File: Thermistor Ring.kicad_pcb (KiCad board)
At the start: 2 copper layers, 48.3 x 48.3 mm, 15 parts, among them J1 Conn_01x04_Socket, U2 MCP9808T-E/MC, U3 MCP9808T-E/MC, U4 MCP9808T-E/MC, U5 MCP9808T-E/MC, U6 MCP9808T-E/MC, U7 MCP9808T-E/MC

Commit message: Ouptut adjustments
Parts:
- U2, U3, U4, U5, U6, U7: footprint MCP9808-E/MS:MSOP8_MC_MCH -> MCP9808-E/MS:MSOP8_MC_MCH_SMALL_PADS
- moved C1 2.72 mm to (77.9, 76.2)
- moved R3 2.46 mm to (58.7, 41.2)
- moved C5 2.02 mm to (59.5, 70.2)
- moved C6 1.95 mm to (93.0, 62.8)
- moved U6 1.24 mm to (64.2, 73.4)
- moved U4 1.24 mm to (83.4, 73.5)
- moved C3 1.24 mm to (63.6, 37.5)
- moved U3 1.24 mm to (54.6, 57.0)
- moved C4 1.24 mm to (87.5, 43.2)
- moved U7 1.24 mm to (83.2, 40.5)
- moved J1 1.24 mm to (69.9, 37.7)
- moved U2 1.24 mm to (64.2, 40.4)
- moved U5 1.24 mm to (92.8, 57.0)
- moved R2 1.10 mm to (82.8, 36.4), turned to 180 degrees
- moved C2 1.06 mm to (54.7, 52.1)
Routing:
- net /Power 3.3-5V: track 204.1 -> 213.8 mm
- net /SCL: track 123.0 -> 124.4 mm
- net /SDA: track 169.3 -> 170.2 mm
- net GND: vias 77 -> 79

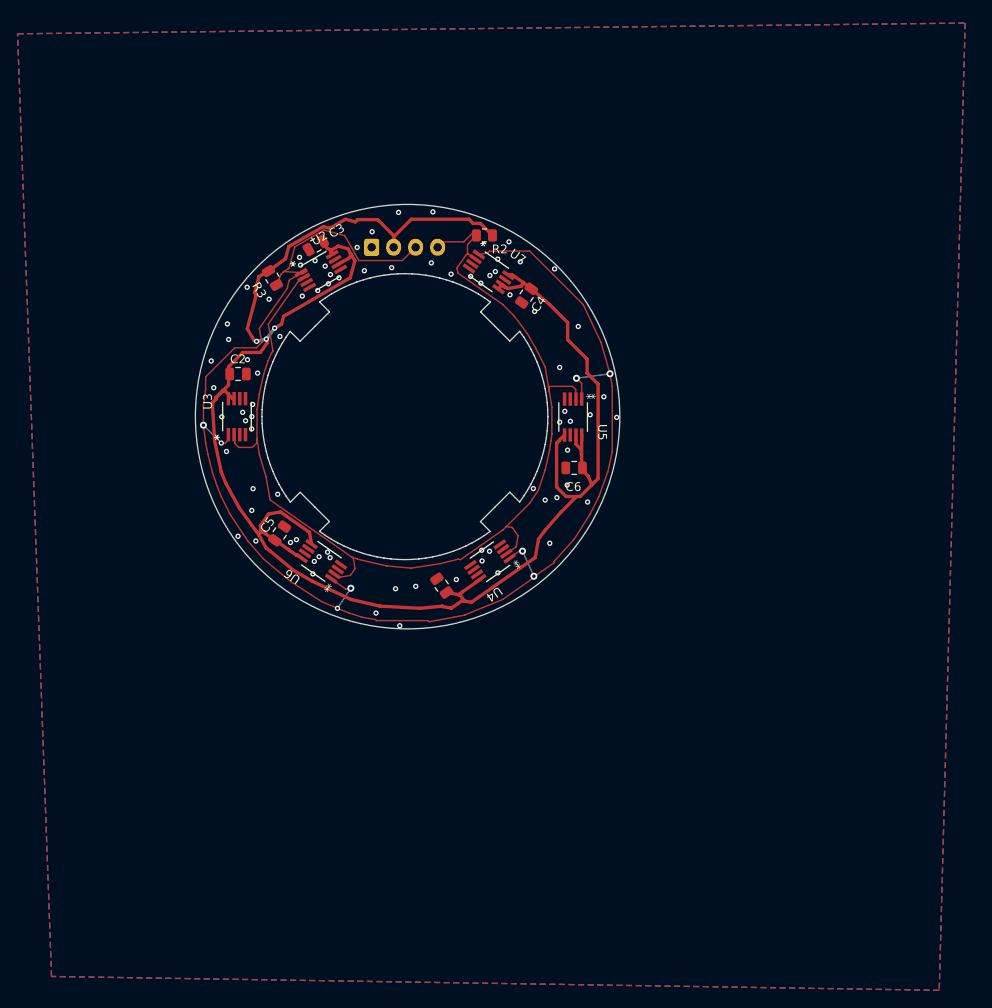
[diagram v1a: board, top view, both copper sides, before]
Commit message: Updated PCB for 8 thermistors
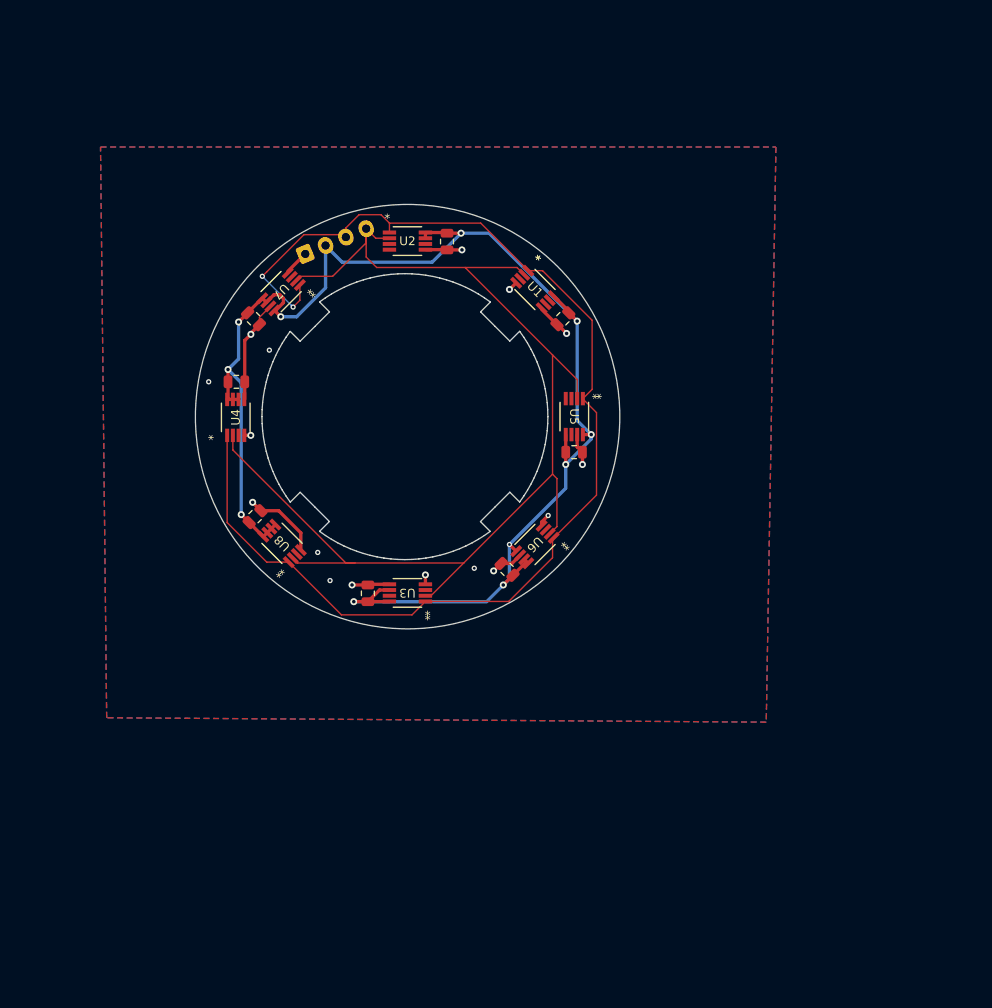
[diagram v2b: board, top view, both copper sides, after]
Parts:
- removed R2, R3: 4.7k, Resistor_SMD:R_0805_2012Metric
- added C7: 0.1uF, Capacitor_SMD:C_0805_2012Metric, F.Cu at (56.5, 45.8)
- added C8: 0.1uF, Capacitor_SMD:C_0805_2012Metric, F.Cu at (56.7, 68.3)
- added U1: MCP9808T-E/MC, MCP9808:MSOP8_MC_MCH, F.Cu at (88.5, 42.5)
- added U8: MCP9808T-E/MC, MCP9808:MSOP8_MC_MCH, F.Cu at (59.7, 71.4)
- U2, U3, U4, U5, U6, U7: footprint MCP9808-E/MS:MSOP8_MC_MCH_SMALL_PADS -> MCP9808:MSOP8_MC_MCH
- moved C3 40.0 mm to (69.5, 77.0), turned to 90 degrees
- moved C5 34.7 mm to (93.0, 61.0), turned to 0 degrees
- moved C4 34.4 mm to (54.5, 53.0), turned to 0 degrees
- moved C1 33.3 mm to (91.7, 45.8), turned to -135 degrees
- moved U4 33.3 mm to (54.5, 57.0), turned to 90 degrees
- moved C2 28.1 mm to (78.5, 37.0), turned to -90 degrees
- moved U3 27.9 mm to (74.0, 77.0), turned to 180 degrees
- moved U6 24.4 mm to (88.5, 71.5), turned to -135 degrees
- moved U7 23.7 mm to (59.6, 42.7), turned to -135 degrees
- moved C6 13.8 mm to (85.3, 74.3), turned to 135 degrees
- moved U2 10.4 mm to (74.0, 37.0), turned to 0 degrees
- moved J1 7.59 mm to (62.4, 38.5), turned to 22.5 degrees
- moved U5 0.14 mm to (93.0, 57.0)
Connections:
- C1 pad 1: /Power 3.3-5V -> VCC
- C2 pad 1: /Power 3.3-5V -> VCC
- C3 pad 1: /Power 3.3-5V -> VCC
- C4 pad 1: /Power 3.3-5V -> VCC
- C5 pad 1: /Power 3.3-5V -> VCC
- C6 pad 1: /Power 3.3-5V -> VCC
- J1 pad 2: /Power 3.3-5V -> VCC
- U2 pad 6: /Power 3.3-5V -> GND
- U2 pad 7: GND -> VCC
- U2 pad 8: /Power 3.3-5V -> VCC
- U3 pad 6: GND -> VCC
- U3 pad 7: /Power 3.3-5V -> GND
- U3 pad 8: /Power 3.3-5V -> VCC
- U4 pad 6: GND -> VCC
- U4 pad 7: GND -> VCC
- U4 pad 8: /Power 3.3-5V -> VCC
- U5 pad 5: /Power 3.3-5V -> VCC
- U5 pad 7: /Power 3.3-5V -> GND
- U5 pad 8: /Power 3.3-5V -> VCC
- U6 pad 5: /Power 3.3-5V -> VCC
- U6 pad 7: GND -> VCC
- U6 pad 8: /Power 3.3-5V -> VCC
- U7 pad 5: /Power 3.3-5V -> VCC
- U7 pad 6: /Power 3.3-5V -> VCC
- U7 pad 8: /Power 3.3-5V -> VCC
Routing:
- net /Power 3.3-5V: track 213.8 -> 0.00 mm, vias 3 -> 0
- net VCC: track 0.00 -> 168.0 mm, vias 0 -> 11
- net GND: track 0.00 -> 48.3 mm, vias 79 -> 11
- net /SDA: track 170.2 -> 139.5 mm, vias 8 -> 2
- net /SCL: track 124.4 -> 138.3 mm
- net (no net): vias 0 -> 5

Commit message: Update layout
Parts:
- turned C5 to 180 degrees
- turned C7 to 135 degrees
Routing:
- net /SCL: track 138.3 -> 118.2 mm
- net GND: track 48.3 -> 37.7 mm, vias 11 -> 12
- net VCC: track 168.0 -> 170.1 mm
- net (no net): vias 5 -> 15
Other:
- board text added: "A"
- board text added: "B"
- board text added: "C"
- board text added: "D"
- board text added: "E"
- board text added: "F"
- board text added: "G"
- board text added: "GND"
- board text added: "H"
- board text added: "SCL"
- board text added: "SDA"
- board text added: "VCC"
- board text added: "____/\\\\\\\\\________/\\\\\\\\\______/\\\\\\\\\\\__/\\\________/\\\_ __/\\\///////\\\____/\\\///////\\\___\/////\\\///__\/\\\_______\/\\\_ _\/\\\_____\/\\\___\/\\\_____\/\\\_______\/\\\_____\//\\\______/\\\__ _\/\\\\\\\\\\\/____\/\\\\\\\\\\\/________\/\\\______\//\\\____/\\\___ _\/\\\//////\\\____\/\\\//////\\\________\/\\\_______\//\\\__/\\\____ _\/\\\____\//\\\___\/\\\____\//\\\_______\/\\\___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"

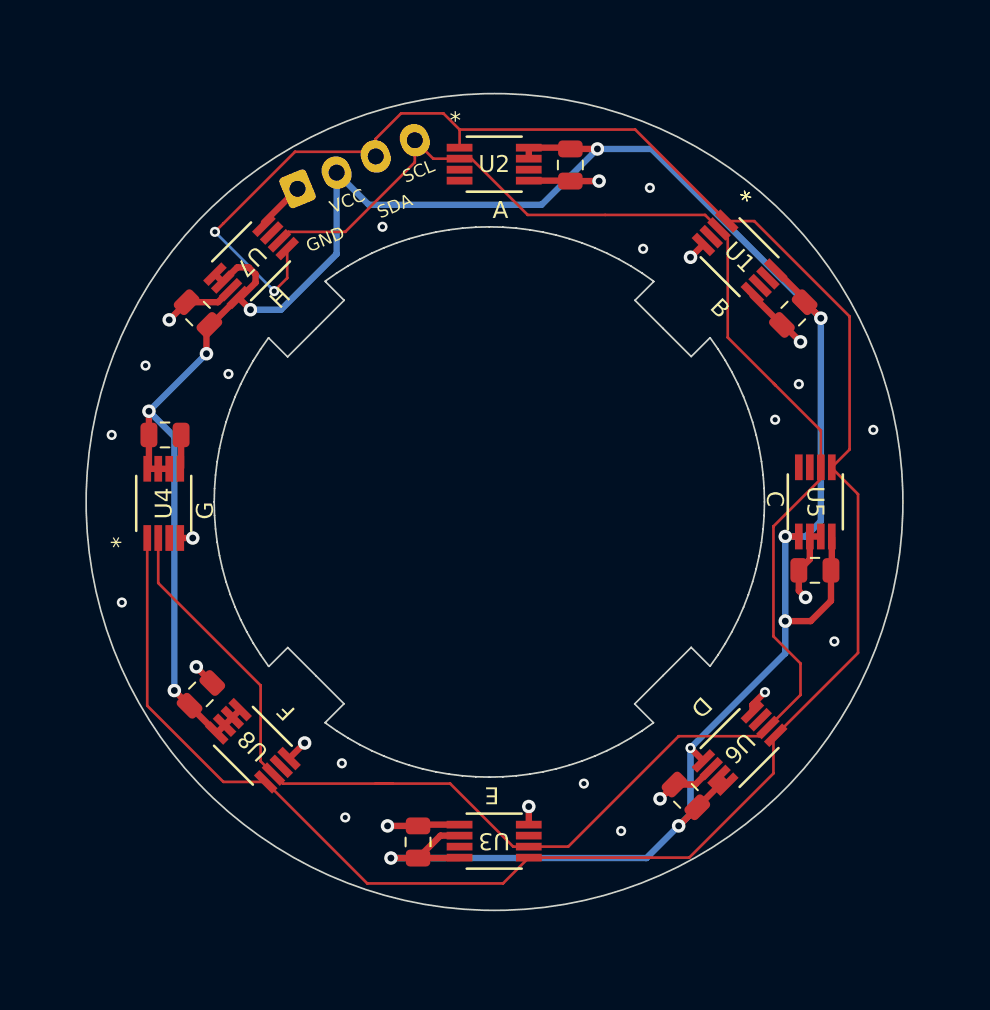
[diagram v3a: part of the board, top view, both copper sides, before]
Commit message: Fixed layout issues in V2.0
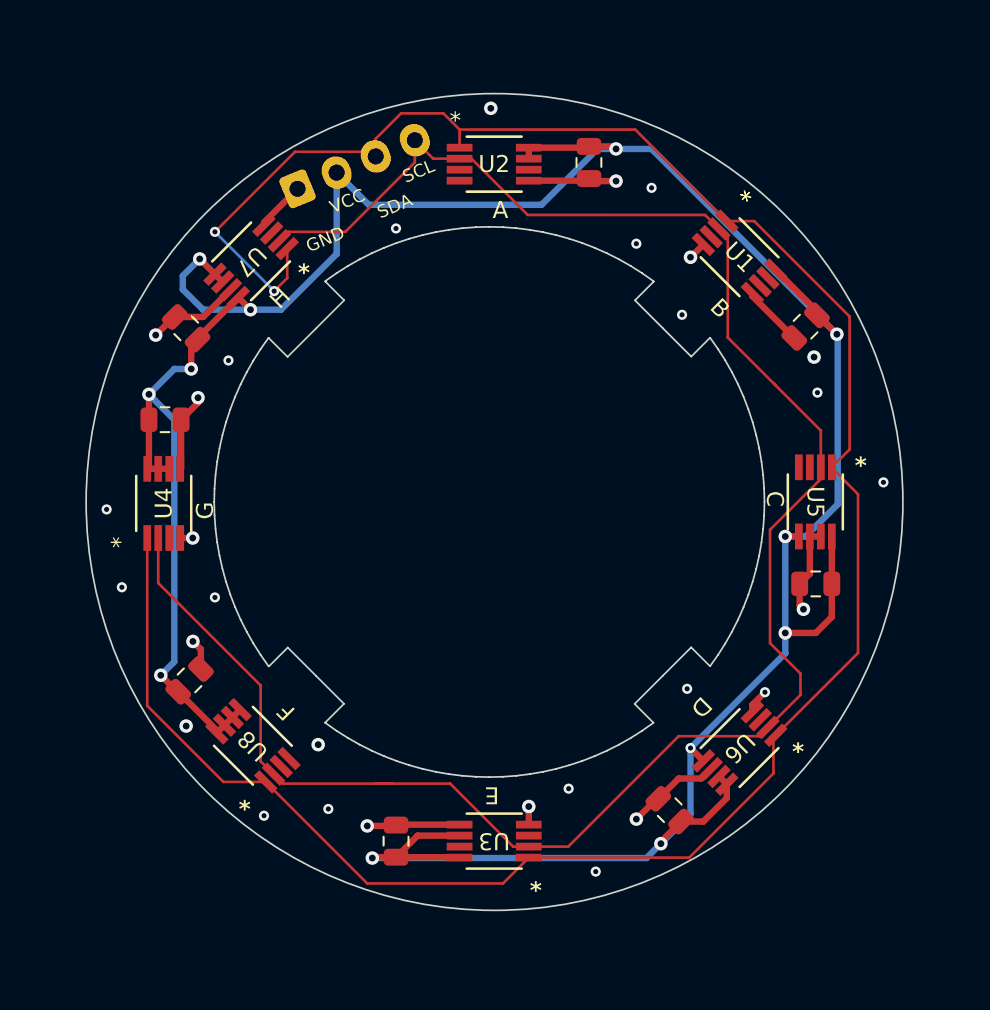
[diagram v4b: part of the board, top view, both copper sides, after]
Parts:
- moved C3 1.30 mm to (68.2, 77.0)
- moved C6 1.28 mm to (84.4, 75.2)
- moved C7 1.12 mm to (55.8, 46.7)
- moved C2 1.11 mm to (79.6, 36.9)
- moved C8 1.07 mm to (56.0, 67.5)
- moved C1 1.06 mm to (92.4, 46.6)
- moved C4 0.90 mm to (54.5, 52.1)
- moved C5 0.80 mm to (93.0, 61.8)
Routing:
- net VCC: track 170.1 -> 186.0 mm, vias 11 -> 12
- net GND: track 37.7 -> 45.6 mm, vias 12 -> 30
- net (no net): vias 15 -> 0
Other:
- board text added: "*"
- board text added: "V2.0"

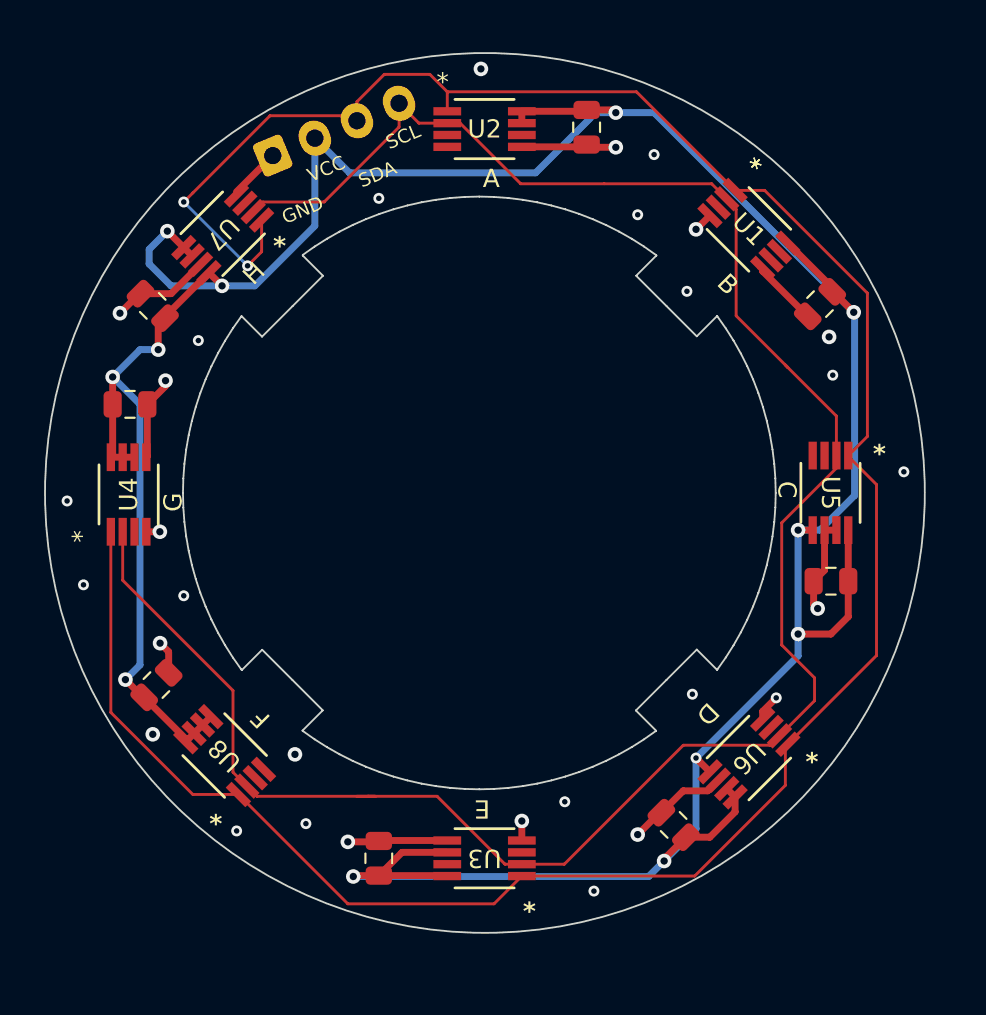
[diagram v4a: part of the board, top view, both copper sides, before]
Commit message: Updated traces and silkscreen
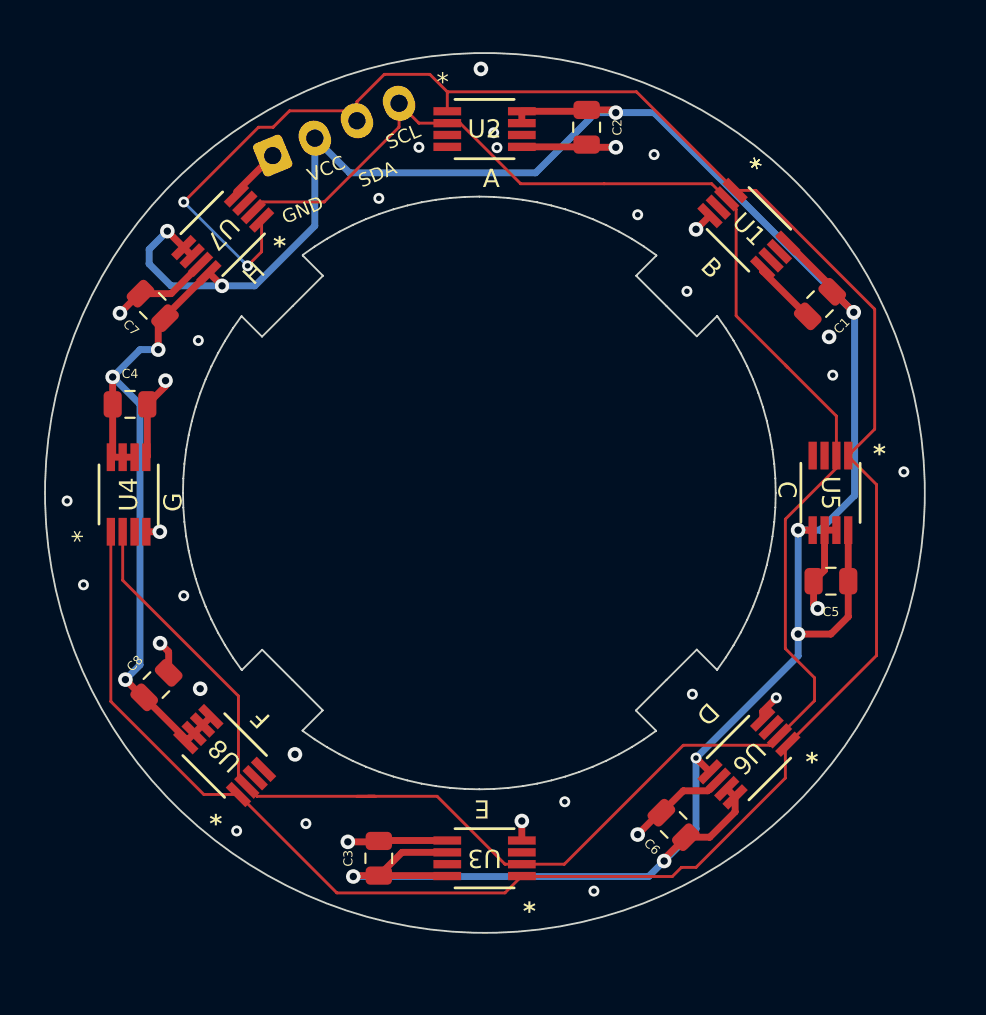
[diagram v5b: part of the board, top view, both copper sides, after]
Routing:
- net /SDA: track 139.5 -> 138.7 mm
- net GND: vias 30 -> 33
